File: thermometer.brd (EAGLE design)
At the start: 100 x 80 mm, 36 parts, among them IC1 MAX232, Q2 54M10AUM1, T1 BC547, T2 BC547, T3 BC547, T6 BC547, T7 BC547, T8 BC547, T9 BC547, X2 MINI-USB_SHIELD4P-85-32004-10X

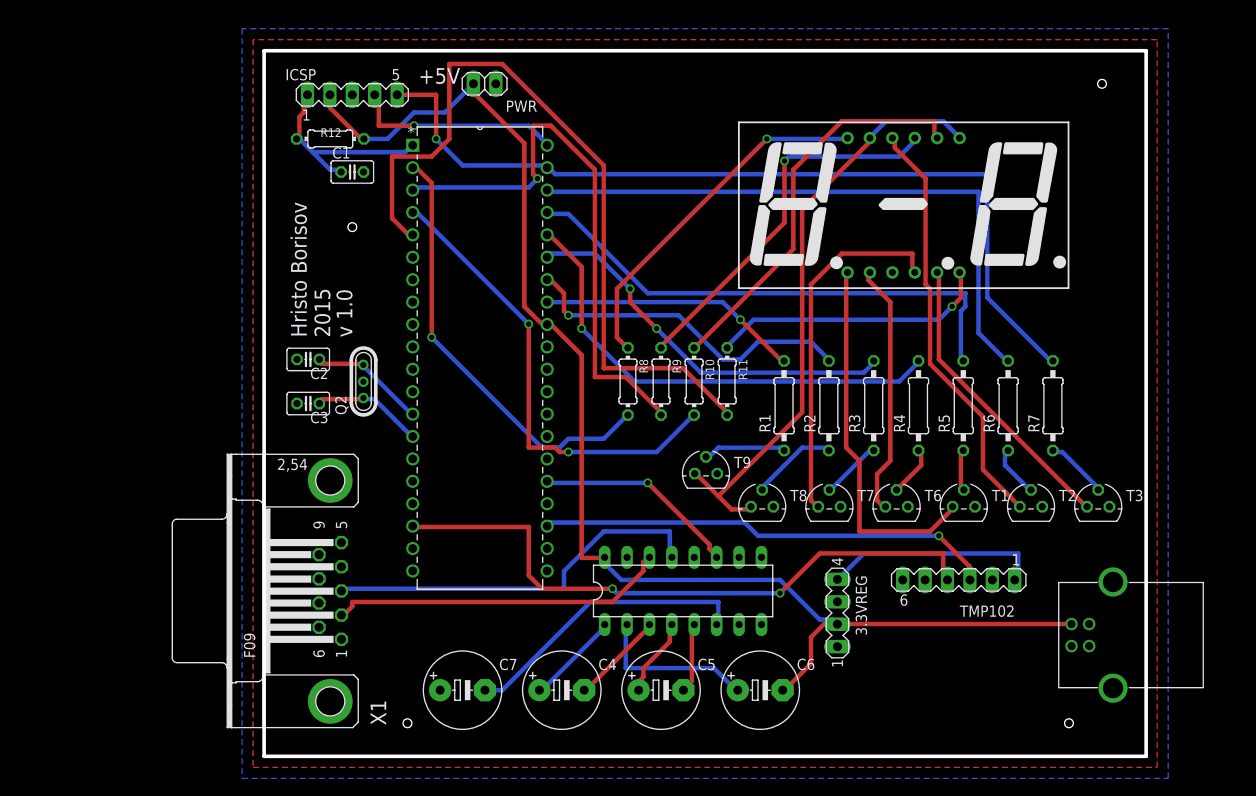
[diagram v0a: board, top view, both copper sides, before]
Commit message: v 1.1 released. Several bug fixes
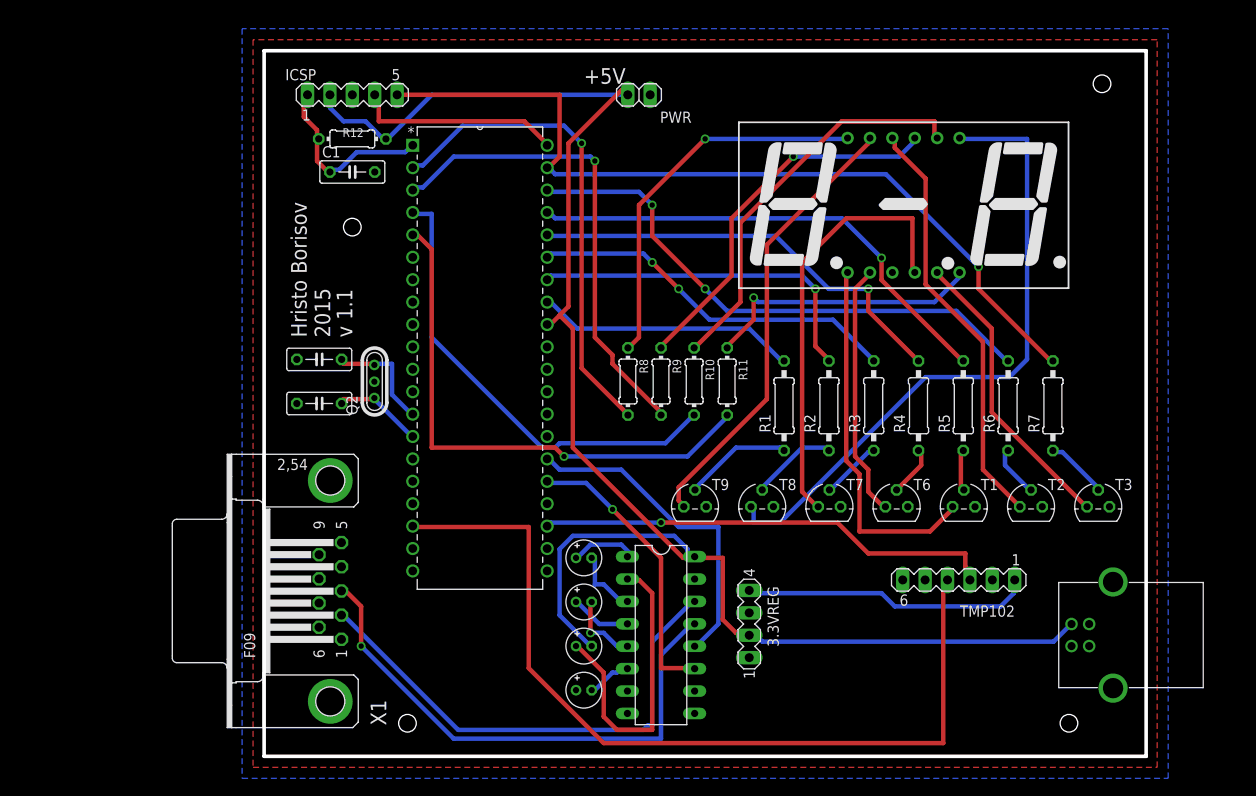
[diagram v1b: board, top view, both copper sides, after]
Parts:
- C1: value (none) -> 100 nF; device rcl:C025-025X050 -> rcl:C050-025X075
- C2, C3: value (none) -> 22 pF; device rcl:C025-025X050 -> rcl:C050-025X075
- C4, C5, C6, C7: value (none) -> 1 uF; device rcl:E5-8,5 -> rcl:E1,8-4
- Q2: value 54M10AUM1 -> 4 MHz
- R12, R2, R3, R4, R5, R6, R7: value (none) -> 10 K
- moved C6 20.6 mm to (36.2, 12.5)
- moved PWR 17.5 mm to (42.5, 75.0)
- moved C4 15.2 mm to (36.2, 22.5)
- moved C7 13.8 mm to (36.2, 7.50)
- moved C5 13.3 mm to (36.2, 17.5)
- moved 3.3VREG 10.1 mm to (55.0, 15.0)
- moved IC1 5.59 mm to (45.0, 13.8), turned to 270 degrees
- moved T9 3.95 mm to (48.9, 28.3)
- moved R12 2.50 mm to (10.0, 70.0)
- moved C2 1.25 mm to (6.25, 45.0)
- moved C3 1.25 mm to (6.25, 40.0)
- moved Q2 1.25 mm to (12.5, 42.5)
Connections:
- removed net N$46: X2.4
- new net N$47: T8.3, U$2.7
- net GND: now also X2.4
- net N$23: no longer T8.3, U$2.7
- net N$45: now also PIC16F877A.26
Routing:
- net N$47: track 0.00 -> 73.3 mm
- net N$45: track 0.00 -> 37.3 mm
- net VCC: track 152.2 -> 186.6 mm
- net N$35: track 33.3 -> 5.10 mm
- net N$33: track 71.9 -> 98.7 mm, vias 2 -> 0
- net N$18: track 87.7 -> 61.7 mm, vias 0 -> 1
- net N$43: track 38.5 -> 57.0 mm
- net N$23: track 67.7 -> 51.0 mm
- net N$44: track 44.2 -> 60.8 mm, vias 0 -> 1
- net N$37: track 18.7 -> 34.5 mm
- net N$42: track 23.1 -> 32.8 mm
- net N$16: track 63.0 -> 54.4 mm
- net N$25: track 40.8 -> 49.4 mm
- net N$32: track 25.4 -> 33.2 mm
- net N$13: track 69.6 -> 62.3 mm, vias 0 -> 2
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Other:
- board text added: "v 1.1"
- board text removed: "v 1.0"

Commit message: Adding schematic and board as images
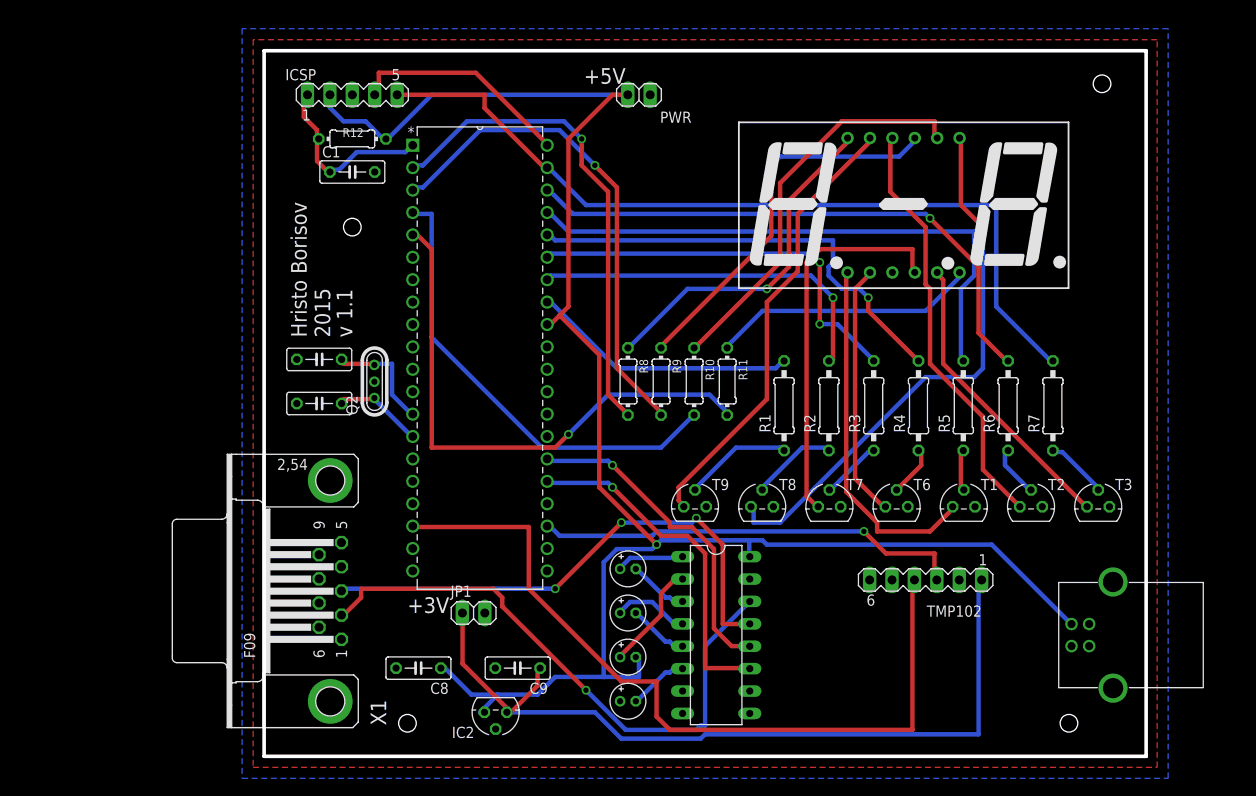
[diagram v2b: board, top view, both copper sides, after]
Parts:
- removed 3.3VREG: (no value), con-lstb:MA04-1
- added C8: .33 uF, rcl:C050-025X075
- added C9: .1 uF, rcl:C050-025X075
- added IC2: 78L05Z, linear:TO92
- added JP1: (no value), pinhead:1X02
- moved IC1 6.25 mm to (51.2, 13.8)
- moved C4 5.15 mm to (41.2, 21.2)
- moved C5 5.15 mm to (41.2, 16.2)
- moved C6 5.15 mm to (41.2, 11.2)
- moved C7 5.15 mm to (41.2, 6.25)
- moved TMP102 3.75 mm to (75.0, 20.0)
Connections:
- removed net N$32: 3.3VREG.4, TMP102.1
- new net N$48: C9.1, IC2.1, JP1.1, TMP102.1
- net GND: now also C8.2, C9.2, IC2.2, JP1.2; no longer 3.3VREG.3
- net VCC: now also C8.1, IC2.3; no longer 3.3VREG.2
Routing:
- net N$48: track 0.00 -> 93.1 mm
- net N$32: track 33.2 -> 0.00 mm
- net N$37: track 34.5 -> 12.6 mm
- net VCC: track 186.6 -> 203.5 mm, vias 0 -> 1
- net N$47: track 73.3 -> 62.4 mm, vias 0 -> 1
- net N$43: track 57.0 -> 66.6 mm, vias 0 -> 1
- net N$12: track 55.6 -> 64.7 mm, vias 1 -> 0
- net N$33: track 98.7 -> 89.9 mm
- net N$42: track 32.8 -> 39.3 mm
- net N$25: track 49.4 -> 43.7 mm
- net N$19: track 43.5 -> 39.4 mm
- net N$10: track 42.3 -> 46.4 mm
- net N$34: track 52.2 -> 48.8 mm
- net N$11: track 49.4 -> 51.9 mm
- net N$13: track 62.3 -> 64.6 mm, vias 2 -> 1
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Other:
- board text added: "+3V"

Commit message: Version 2.0 with TCN75 and USB Micro B
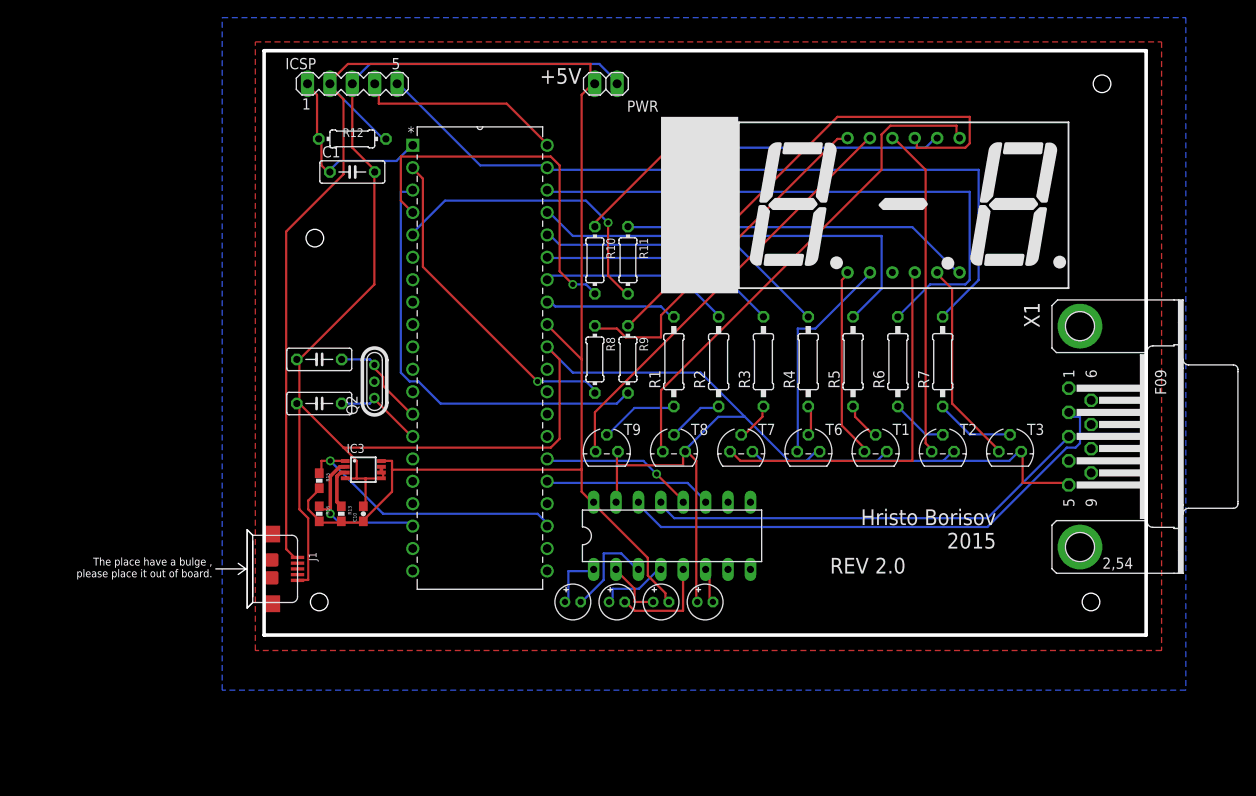
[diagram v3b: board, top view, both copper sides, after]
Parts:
- removed C8: .33 uF, rcl:C050-025X075
- removed C9: .1 uF, rcl:C050-025X075
- removed IC2: 78L05Z, linear:TO92
- removed JP1: (no value), pinhead:1X02
- removed TMP102: (no value), con-lstb:MA06-1
- removed X2: MINI-USB_SHIELD4P-85-32004-10X, con-cypressindustries:85-32004-10X
- added C10: 0.1uF, SparkFun-Capacitors:0603-CAP
- added IC3: (no value), instruction_set:MSOP8
- added J1: MICRO-USB-5P-340015001, Connector:B-SMD-5P
- added R13, R15, R16: 10K, SparkFun-Resistors:0603-RES
- moved X1 86.8 mm to (92.5, 36.2), turned to 270 degrees
- moved R10 17.8 mm to (37.5, 56.2)
- moved R11 17.8 mm to (41.2, 56.2)
- moved C7 14.3 mm to (50.0, 17.5)
- moved R1 13.5 mm to (46.5, 44.8)
- moved R2 13.5 mm to (51.5, 44.8)
- moved R3 13.5 mm to (56.6, 44.8)
- moved R4 13.5 mm to (61.7, 44.8)
- moved R5 13.5 mm to (66.8, 44.8)
- moved R6 13.5 mm to (71.8, 44.8)
- moved R7 13.5 mm to (76.9, 44.8)
- moved IC1 12.3 mm to (46.2, 25.0), turned to 0 degrees
- moved T1 11.8 mm to (69.3, 34.5)
- moved T2 11.8 mm to (77.0, 34.5)
- moved T3 11.8 mm to (84.6, 34.5)
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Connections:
- removed net N$34: PIC16F877A.23, TMP102.3
- removed net N$48: C9.1, IC2.1, JP1.1, TMP102.1
- new net N$32: IC3.2, PIC16F877A.18, R16.1
- new net N$49: IC3.3, R13.1
- net GND: now also C10.2, IC3.4, IC3.5, IC3.6, IC3.7, J1.5; no longer C8.2, C9.2, IC2.2, JP1.2, TMP102.2, TMP102.6, X2.4
- net N$33: now also IC3.1, PIC16F877A.23, R15.1; no longer PIC16F877A.18, TMP102.4
- net VCC: now also C10.1, IC3.8, J1.1, R13.2, R15.2, R16.2; no longer C8.1, IC2.3, X2.1
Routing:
- net GND: track 0.00 -> 270.8 mm
- net N$48: track 93.1 -> 0.00 mm
- net N$33: track 89.9 -> 32.0 mm, vias 0 -> 1
- net N$34: track 48.8 -> 0.00 mm, vias 1 -> 0
- net N$18: track 62.9 -> 34.0 mm
- net N$42: track 39.3 -> 19.0 mm, vias 1 -> 0
- net N$45: track 37.3 -> 17.5 mm
- net N$9: track 41.2 -> 21.7 mm, vias 1 -> 0
- net N$27: track 40.7 -> 21.6 mm
- net N$10: track 46.4 -> 27.3 mm, vias 2 -> 0
- net N$11: track 51.9 -> 33.4 mm, vias 1 -> 0
- net N$15: track 55.7 -> 37.3 mm
- net N$32: track 0.00 -> 17.8 mm, vias 0 -> 1
- net N$8: track 30.3 -> 15.0 mm
- net N$12: track 64.7 -> 49.5 mm
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- added copper zone on layer 1, net N$34
- removed copper zone on layer 1, net GND
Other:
- board size 100 x 80 mm -> 100 x 66.2 mm
- board text added: "REV 2.0"
- board text removed: "+3V"
- board text removed: "v 1.1"

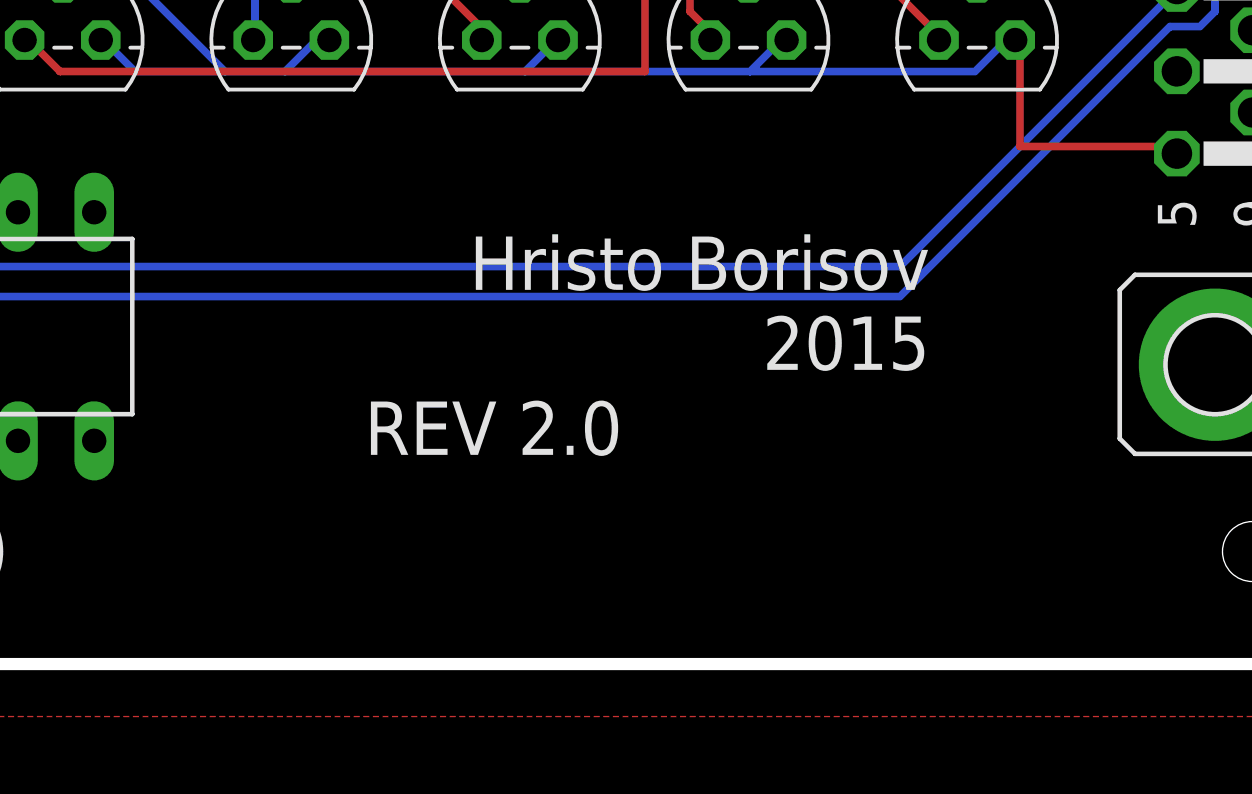
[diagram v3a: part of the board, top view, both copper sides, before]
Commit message: Adding some text and Open Hardware logo
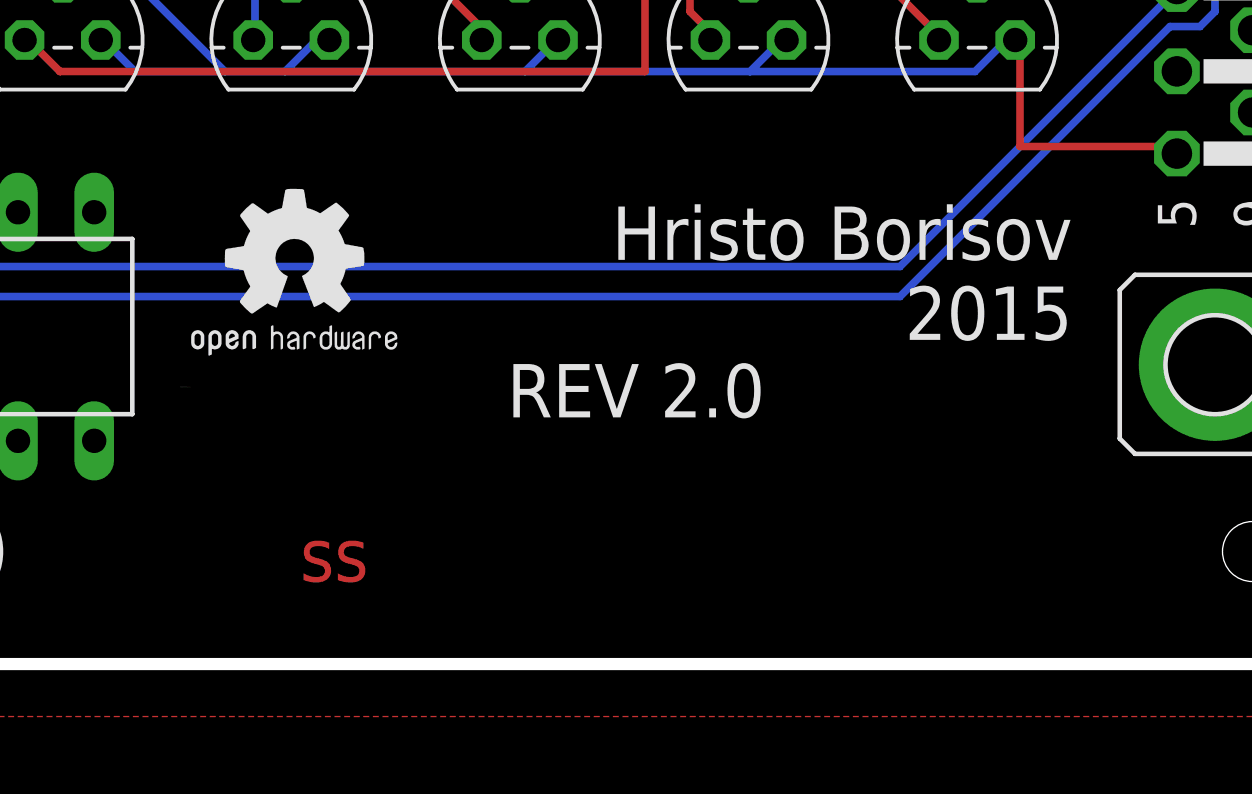
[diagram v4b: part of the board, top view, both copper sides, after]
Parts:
- added GOLD_ORB_SM1: OSHWLOGO_GOLD_ORB_LG, NBitWonder:OSHW0
- added GOLD_ORB_SM2: OSHWLOGO_GOLD_ORB_SM, NBitWonder:OSHW2
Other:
- board text added: "https://github.com/hborisov/thermometer"
- board text added: "ss"
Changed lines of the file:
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@@
 <board>
 <plain>
-<text x="72.75" y="22.5" size="1.778" layer="25" rot="R180">REV 2.0</text>
+<text x="77.5" y="23.75" size="1.778" layer="25" rot="R180">REV 2.0</text>
 <hole x="6.25" y="17.5" drill="2"/>
 <hole x="5.75" y="58.75" drill="2"/>
@@
 <hole x="95" y="76.25" drill="2"/>
 <hole x="93.75" y="17.5" drill="2"/>
-<text x="83" y="28" size="1.778" layer="25" rot="R180">Hristo Borisov
+<text x="87.75" y="29" size="1.778" layer="25" rot="R180">Hristo Borisov
 2015</text>
 <text x="31.25" y="76.25" size="1.778" layer="25">+5V</text>
 <rectangle x1="45" y1="52.5" x2="53.75" y2="72.5" layer="25"/>
+<text x="62" y="16.5" size="1.778" layer="1">ss</text>
+<text x="98" y="53" size="1.778" layer="26" rot="MR0">https://github.com/hborisov/thermometer</text>
 </plain>
 <attributes>
@@
 </element>
 <element name="J1" library="Connector" package="B-SMD-5P" value="MICRO-USB-5P-340015001" x="1.25" y="21.25" rot="R270"/>
+<element name="GOLD_ORB_SM1" library="NBitWonder" package="OSHW0" value="OSHWLOGO_GOLD_ORB_LG" x="99.75" y="52.75" rot="MR0"/>
+<element name="GOLD_ORB_SM2" library="NBitWonder" package="OSHW2" value="OSHWLOGO_GOLD_ORB_SM" x="58" y="23"/>
 </elements>
 <signals>
